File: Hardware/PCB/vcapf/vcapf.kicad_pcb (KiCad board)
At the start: 2 copper layers, 146 x 171 mm, 67 parts, among them J1 Synth_power_2x5, J2 AudioJack2, J3 AudioJack2, J4 Conn_01x05, J5 Conn_01x05, J6 AudioJack2, J7 AudioJack2, Q1 2N3906, Q2 2N3906, U1 LM13700, U2 TL074, U3 TL072

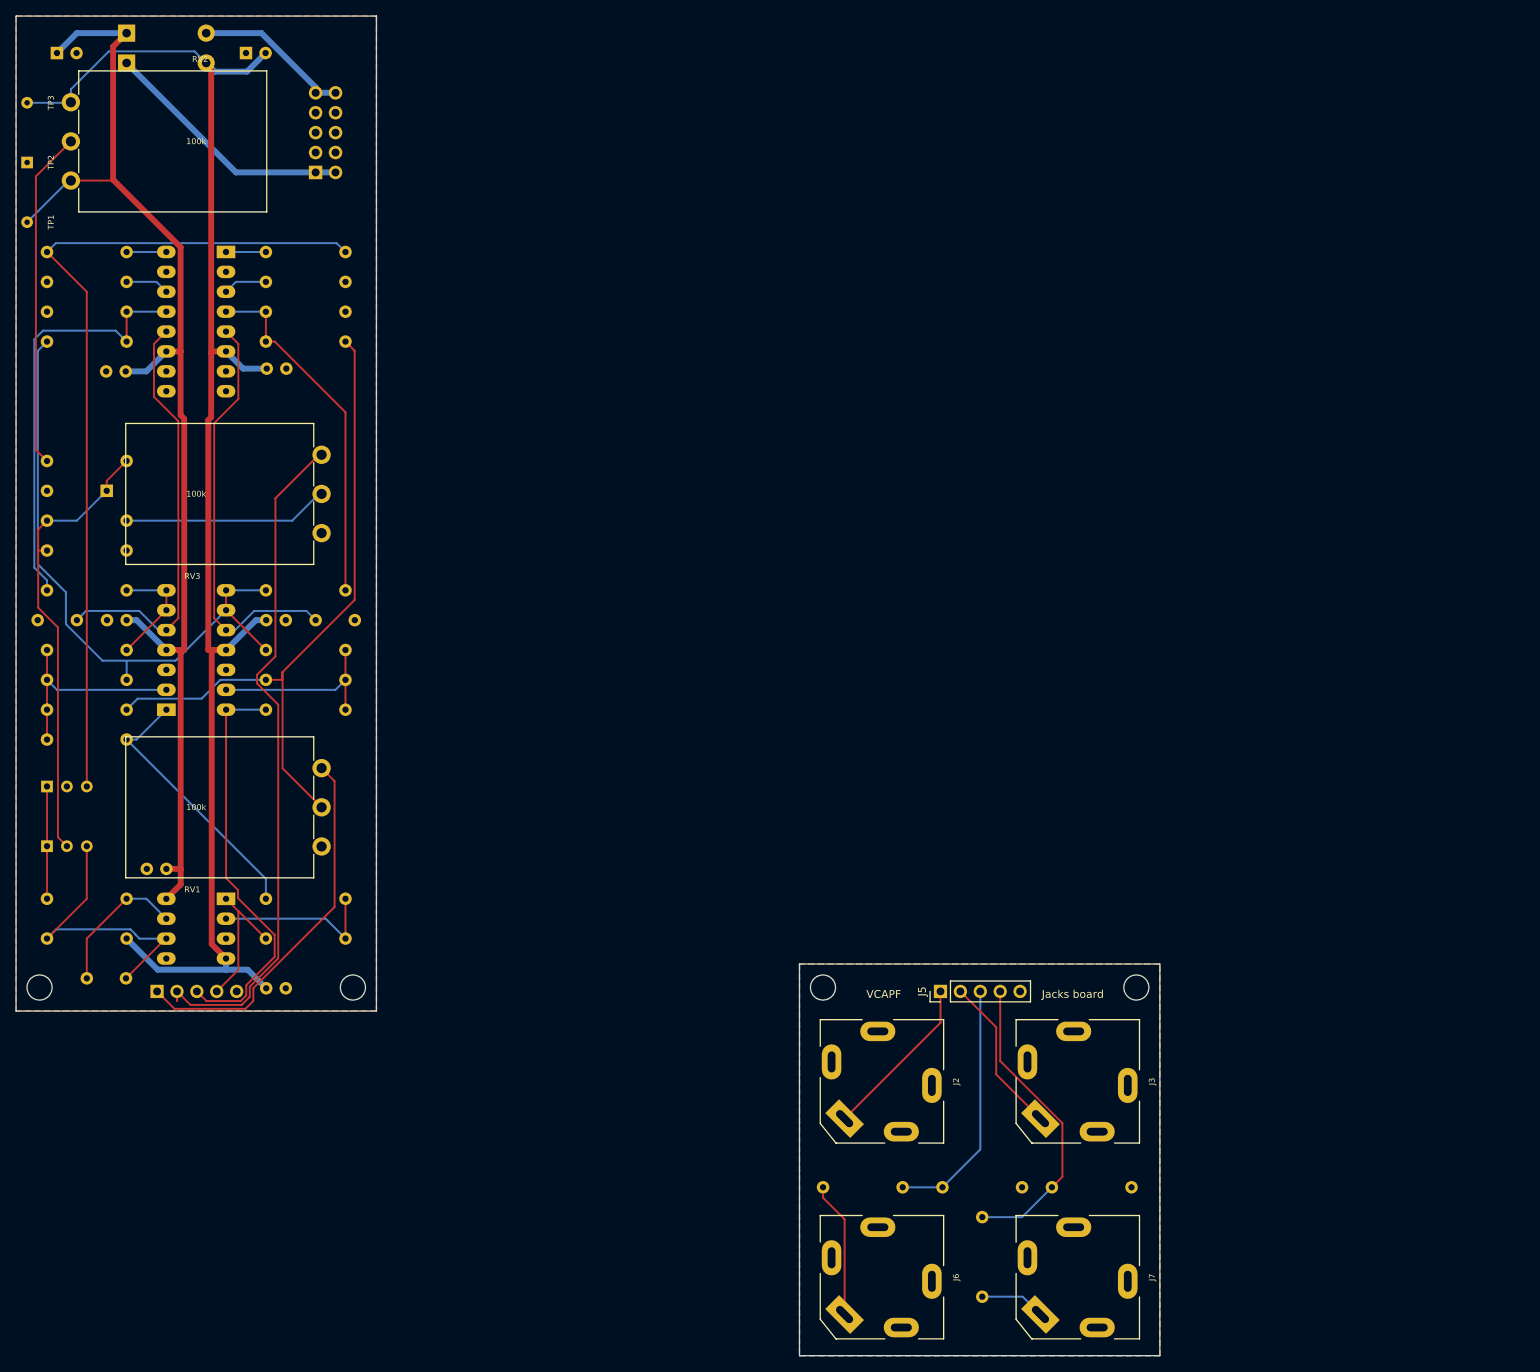
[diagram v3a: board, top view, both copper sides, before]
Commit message: Pre fab tweaks, unreverse jacks, Gerbers
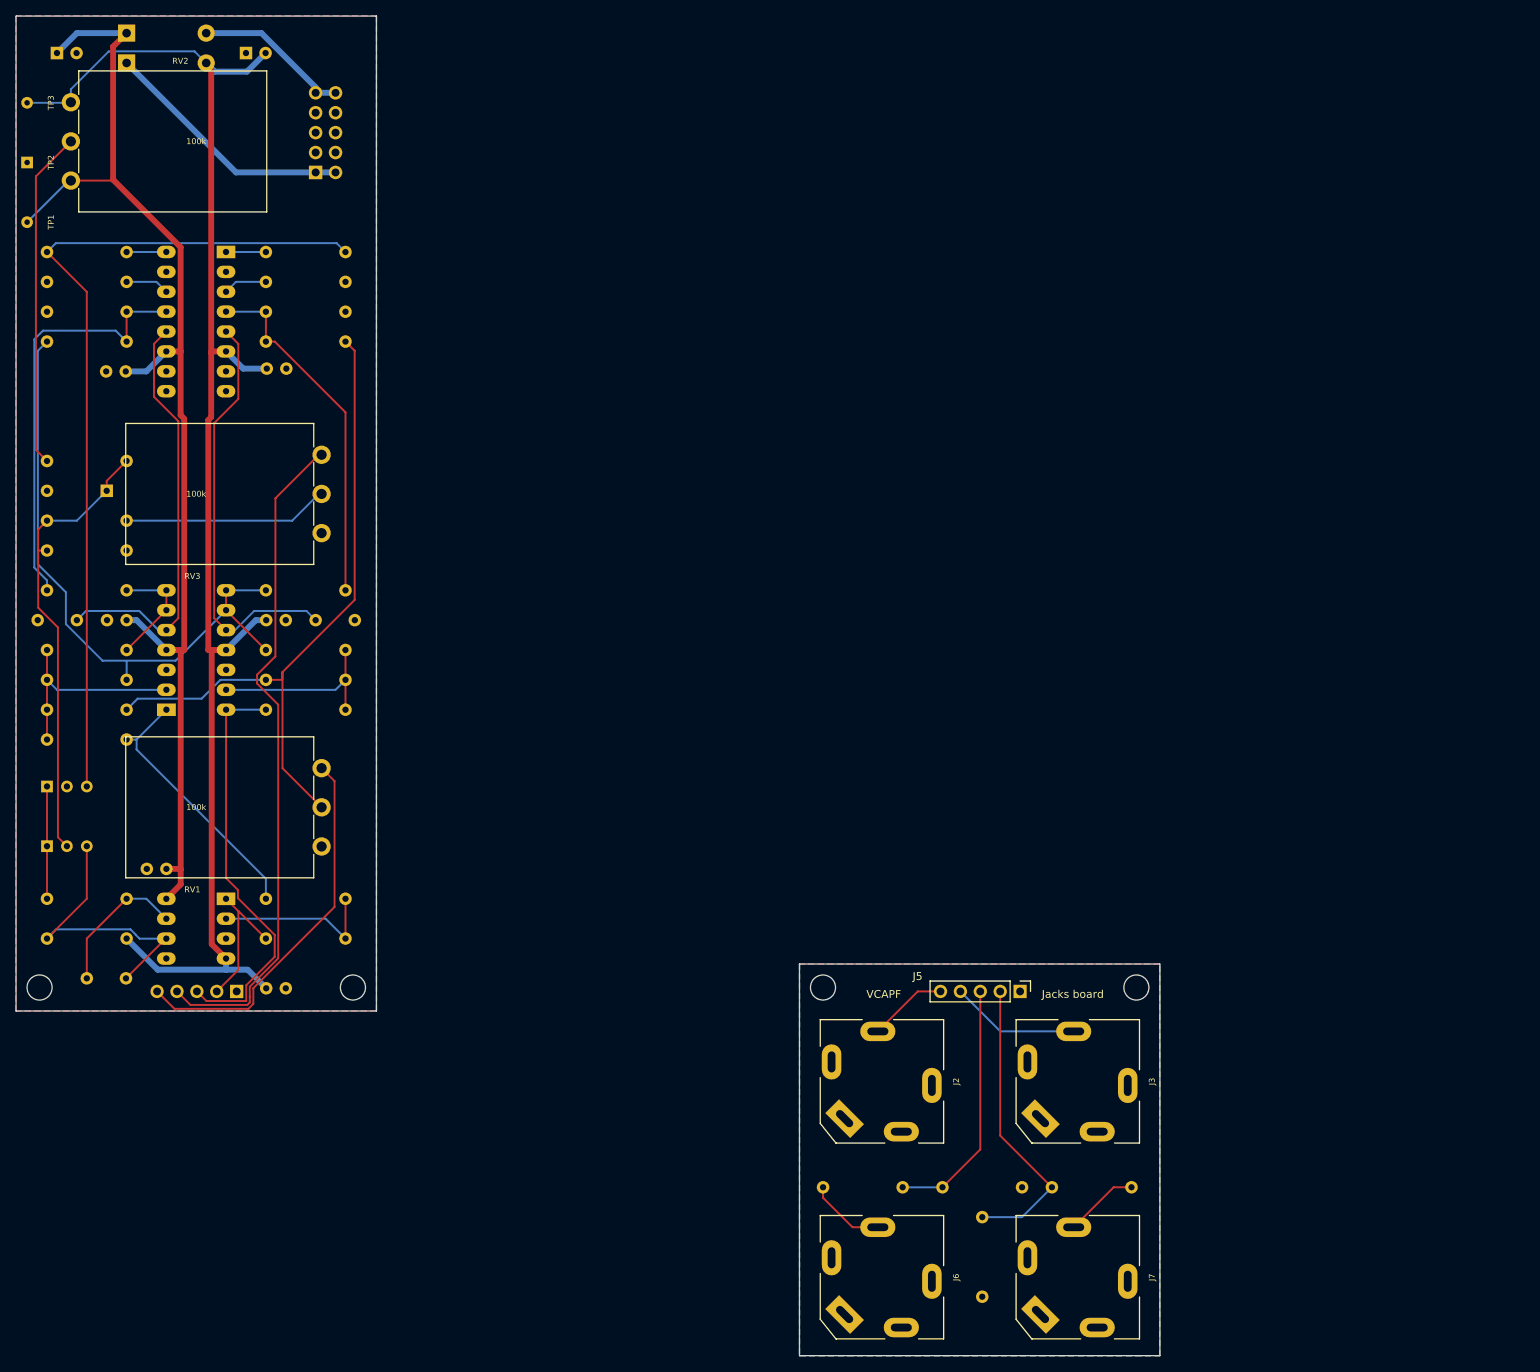
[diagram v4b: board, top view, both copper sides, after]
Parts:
- added B1: Board, ao_tht:Board_Marker, F.Cu at (77.0, 31.0)
- added B2: Board, ao_tht:Board_Marker, F.Cu at (182.5, 135.0)
- Q1, Q2: value 2N3906 -> 2N3906 matched
- moved GRAF1 100.0 mm to (200.0, 100.0)
- moved J4 10.2 mm to (105.2, 138.5), turned to 90 degrees
- moved J5 10.2 mm to (205.2, 138.5), turned to -90 degrees
- moved R2 9.67 mm to (200.3, 167.3), turned to -90 degrees
- moved R4 9.67 mm to (209.2, 163.5), turned to 0 degrees
- renumbered C4 to C3, C5 to C4, C3 to C5, R25 to R1, R6 to R10, R7 to R11, R8 to R12, R9 to R13, R10 to R14, R11 to R15, R12 to R16, R13 to R17, R14 to R18, R15 to R19, R26 to R2, R16 to R20, R17 to R21, R18 to R22, R19 to R23, R20 to R24, R21 to R25, R22 to R26, R23 to R27, R24 to R28, R27 to R3, R28 to R4, R1 to R5, R2 to R6, R3 to R7, R4 to R8, R5 to R9
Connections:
- J2 pad S: /INPUT_J -> GND1
- J2 pad T: GND1 -> /INPUT_J
- J3 pad S: /CV_J -> GND1
- J3 pad T: GND1 -> /CV_J
- J4 pad 1: /Main PCB/INPUT -> GND
- J4 pad 2: /Main PCB/CV_IN -> /Main PCB/2POLE_OUT
- J4 pad 4: /Main PCB/2POLE_OUT -> /Main PCB/CV_IN
- J4 pad 5: GND -> /Main PCB/INPUT
- J5 pad 1: /INPUT_J -> GND1
- J5 pad 2: /CV_J -> /2POLE_OUT_J
- J5 pad 4: /2POLE_OUT_J -> /CV_J
- J5 pad 5: GND1 -> /INPUT_J
- J6 pad S: /1P OUT -> GND1
- J6 pad T: GND1 -> /1P OUT
- J7 pad S: /2P OUT -> GND1
- J7 pad T: GND1 -> /2P OUT
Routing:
- net /INPUT_J: track 21.3 -> 10.1 mm
- net /1P OUT: track 17.4 -> 9.89 mm
- net /CV_J: track 20.5 -> 16.6 mm
- net /Main PCB/CV_IN: track 88.0 -> 85.9 mm
- net /2P OUT: track 8.37 -> 9.49 mm
- net /2POLE_OUT_J: track 39.3 -> 38.2 mm
- net Net-(C11-Pad1): track 53.6 -> 52.6 mm
- net Net-(R25-Pad1): track 34.3 -> 33.8 mm
